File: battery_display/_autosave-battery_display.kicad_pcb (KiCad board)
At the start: 2 copper layers, 100 x 60 mm, 30 parts, among them J1 FH34SRJ-24S-0.5SH_99_, J2 Screw_Terminal_2x2.54, Q1 ZXM61N03F, Q2 ZXM61N03F, SW1 Button-THT - 2-1825910-7, U1 LDO40LPU33RY

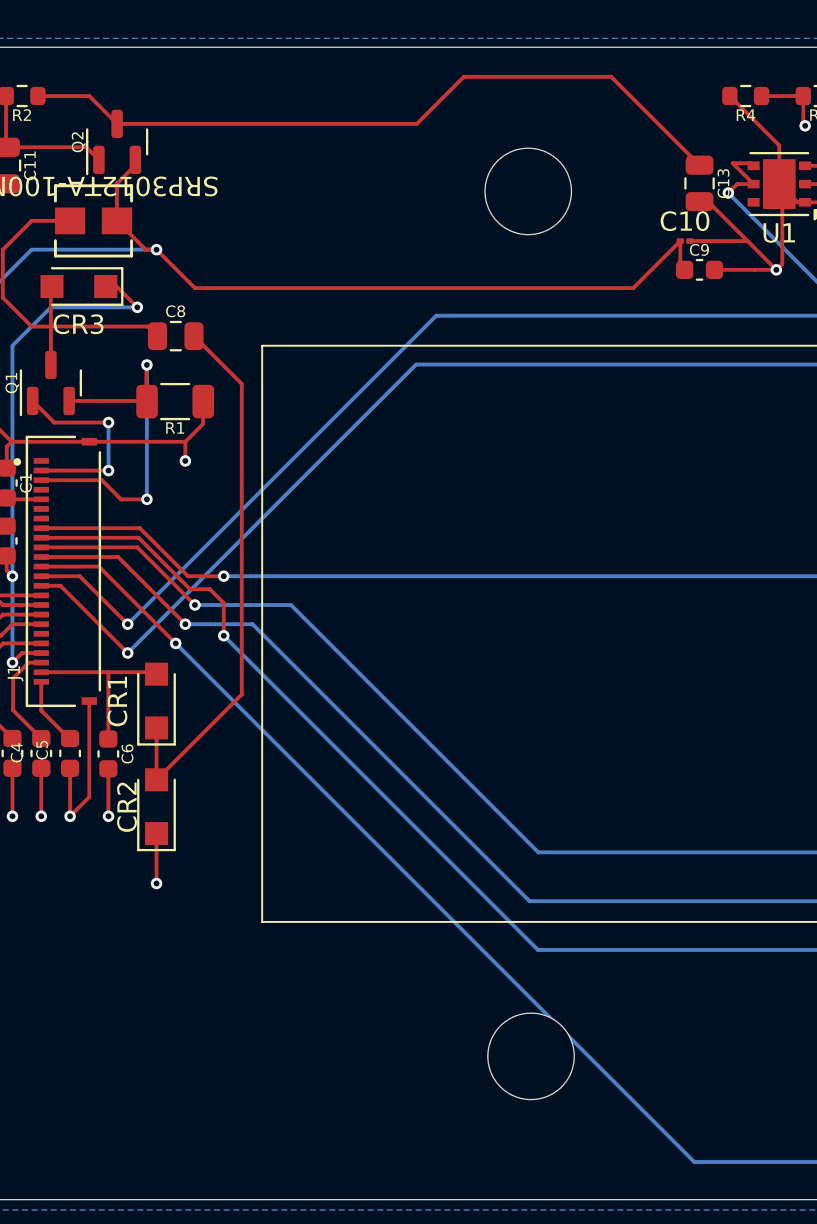
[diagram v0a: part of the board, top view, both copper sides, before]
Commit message: Adjusted drill hole placements (again)
Drill holes moved to be 30mm away from the left edge of the board
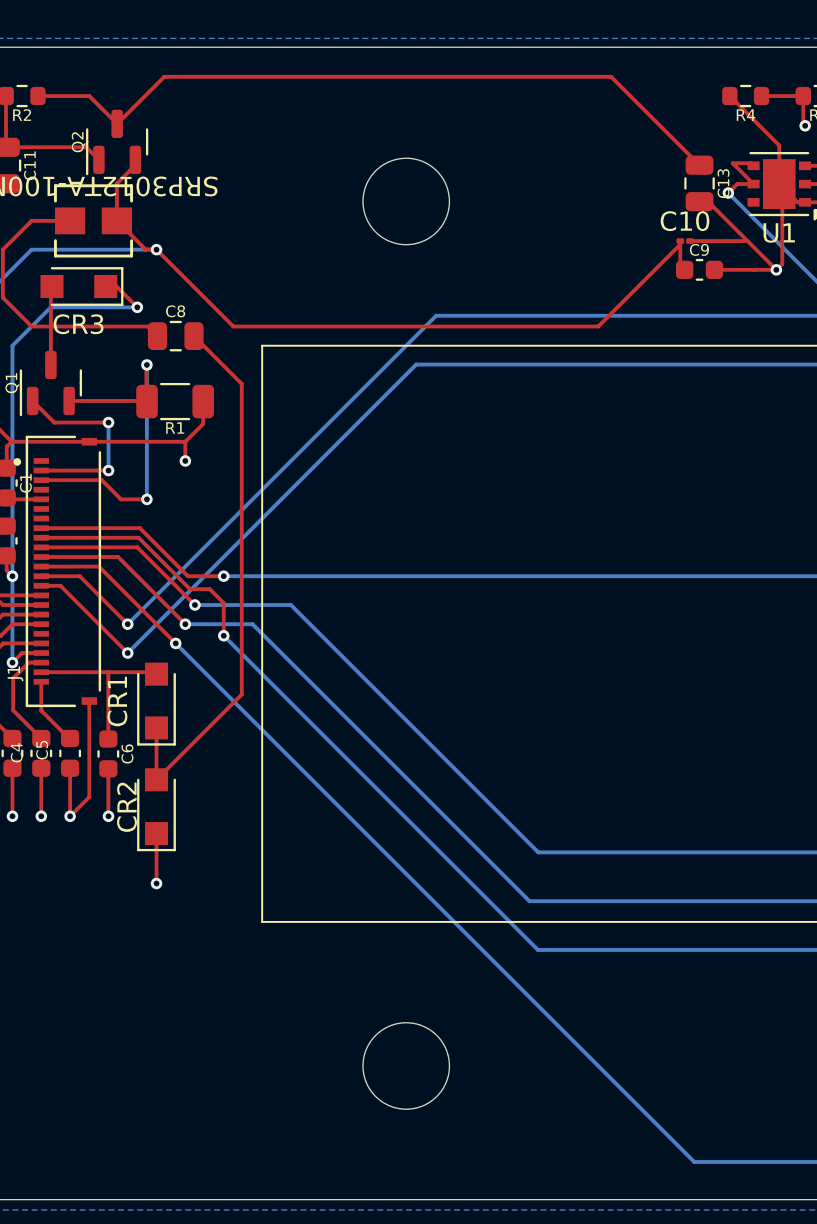
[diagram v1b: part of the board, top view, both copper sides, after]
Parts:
- moved H2 6.52 mm to (178.5, 83.0)
- moved H1 6.37 mm to (178.5, 38.0)
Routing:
- net /Display VDDD: track 67.5 -> 69.3 mm
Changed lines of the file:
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@@
 	(footprint "rsx_misc:MountingHole_4.5mm"
 		(layer "F.Cu")
-		(at 184.852431 37.467366)
+		(at 178.499999 37.989087)
 		(descr "Mounting Hole 4.5mm, no annular")
 		(tags "mounting hole 4.5mm no annular")
@@
 	(footprint "rsx_misc:MountingHole_4.5mm"
 		(layer "F.Cu")
-		(at 185 82.5)
+		(at 178.5 83)
 		(descr "Mounting Hole 4.5mm, no annular")
 		(tags "mounting hole 4.5mm no annular")
@@
 	)
 	(segment
-		(start 166.5 61)
-		(end 193.5 88)
+		(start 245.88 88)
+		(end 251.84 82.04)
 		(width 0.2)
 		(layer "B.Cu")
@@
 	)
 	(segment
-		(start 193.5 88)
-		(end 245.88 88)
+		(start 166.5 61)
+		(end 193.5 88)
 		(width 0.2)
 		(layer "B.Cu")
@@
 	)
 	(segment
-		(start 245.88 88)
-		(end 251.84 82.04)
+		(start 193.5 88)
+		(end 245.88 88)
 		(width 0.2)
 		(layer "B.Cu")
@@
 	)
 	(segment
-		(start 163.45 33.95)
-		(end 179.05 33.95)
+		(start 196.585 37.084)
+		(end 195.738 37.084)
+		(width 0.2)
+		(layer "F.Cu")
+		(net 66)
+	)
+	(segment
+		(start 193.772 36.1)
+		(end 189.172 31.5)
 		(width 0.2)
 		(layer "F.Cu")
@@
 	)
 	(segment
-		(start 196.585 37.084)
-		(end 195.738 37.084)
+		(start 165.9 31.5)
+		(end 163.45 33.95)
 		(width 0.2)
 		(layer "F.Cu")
@@
 	(segment
 		(start 189.172 31.5)
-		(end 193.772 36.1)
+		(end 165.9 31.5)
 		(width 0.2)
 		(layer "F.Cu")
@@
 	)
 	(segment
-		(start 179.05 33.95)
-		(end 181.5 31.5)
-		(width 0.2)
-		(layer "F.Cu")
-		(net 66)
-	)
-	(segment
-		(start 181.5 31.5)
-		(end 189.172 31.5)
-		(width 0.2)
-		(layer "F.Cu")
-		(net 66)
-	)
-	(segment
 		(start 162 32.5)
 		(end 163.45 33.95)
@@
 	)
 	(segment
-		(start 190.322 42.5)
-		(end 192.772 40.05)
+		(start 169.5 44.5)
+		(end 188.5 44.5)
 		(width 0.2)
 		(layer "F.Cu")
@@
 	)
 	(segment
-		(start 159.5 58.5)
-		(end 157 58.5)
+		(start 165.5 40.5)
+		(end 169.5 44.5)
 		(width 0.2)
 		(layer "F.Cu")
@@
 	)
 	(segment
-		(start 157.5 59)
-		(end 159.5 59)
+		(start 159.5 58.5)
+		(end 157 58.5)
 		(width 0.2)
 		(layer "F.Cu")
@@
 	)
 	(segment
-		(start 165.5 40.5)
-		(end 167.5 42.5)
+		(start 157.5 59)
+		(end 159.5 59)
 		(width 0.2)
 		(layer "F.Cu")
@@
 	)
 	(segment
-		(start 164.4 35.825)
-		(end 164.4 36.1)
+		(start 192.772 40.228)
+		(end 192.772 40.05)
 		(width 0.2)
 		(layer "F.Cu")
@@
 	)
 	(segment
-		(start 167.5 42.5)
-		(end 190.322 42.5)
+		(start 164.4 35.825)
+		(end 164.4 36.1)
 		(width 0.2)
 		(layer "F.Cu")
@@
 		(width 0.2)
 		(layer "F.Cu")
+		(net 75)
+	)
+	(segment
+		(start 188.5 44.5)
+		(end 192.772 40.228)
+		(width 0.2)
+		(layer "F.Cu")

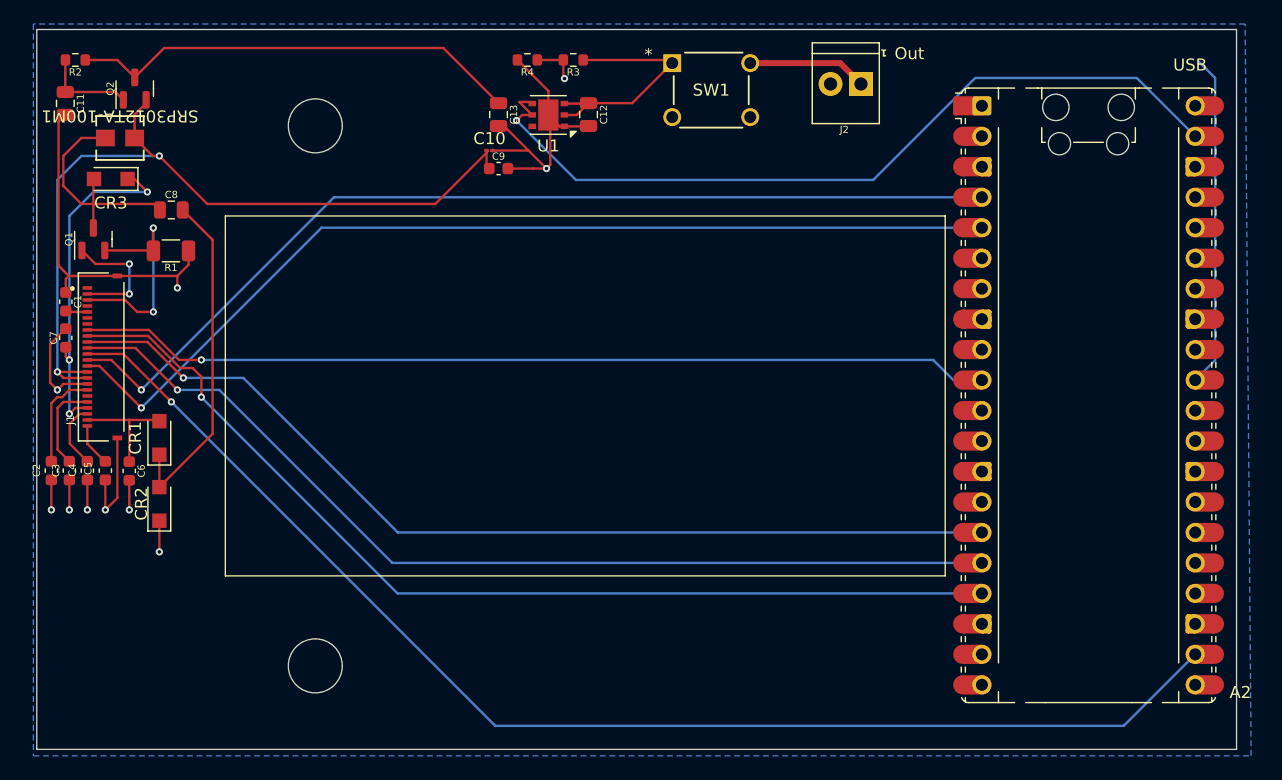
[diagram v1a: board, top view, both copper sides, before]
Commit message: changed wire connections
changed back side wires to front side wires to avoid back side copper islanding
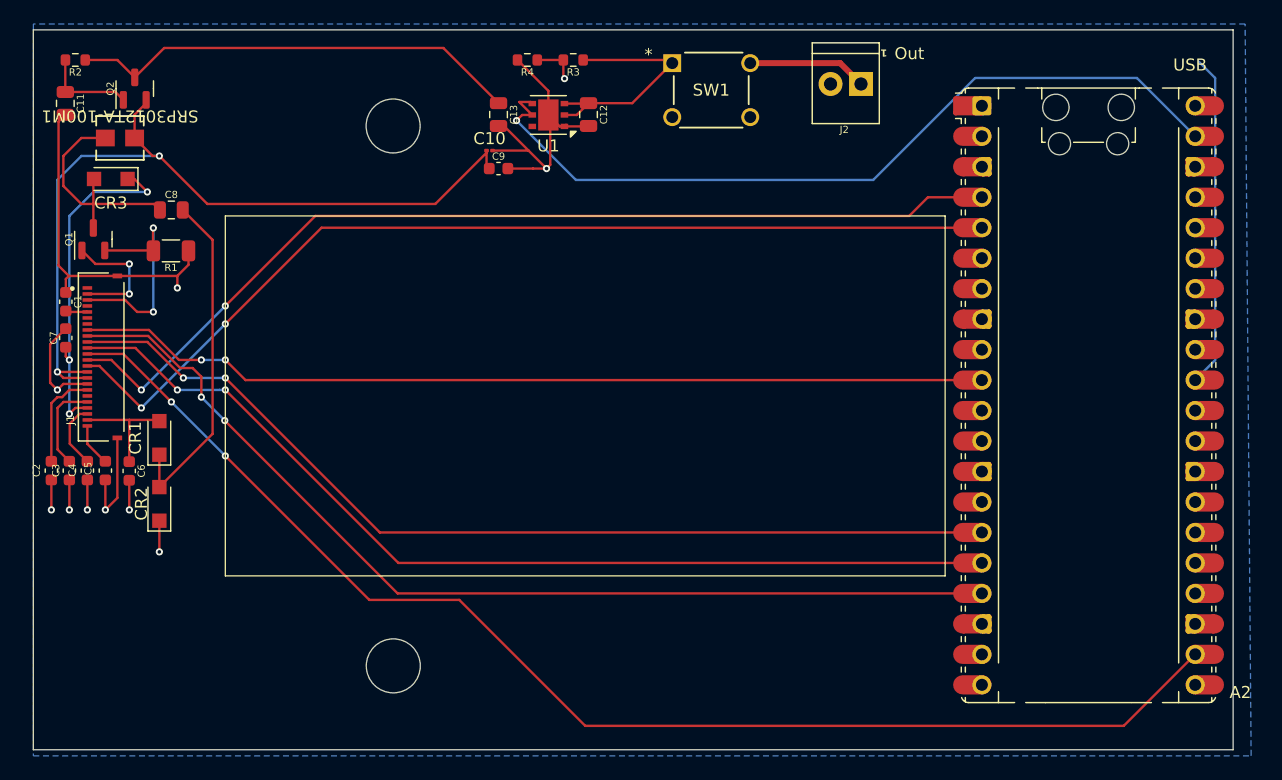
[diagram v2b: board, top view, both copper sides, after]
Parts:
- moved H2 6.50 mm to (185.0, 83.0)
- moved H1 6.48 mm to (185.0, 38.0)
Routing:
- net /BS: track 76.3 -> 78.7 mm, vias 1 -> 2
- net /panelDC: vias 1 -> 2
- net /panelBusy: vias 1 -> 2
- net /panelReset: vias 1 -> 2
- net /panelCS: vias 1 -> 2
- net /SDA: vias 1 -> 2
- net /SCLK: vias 1 -> 2
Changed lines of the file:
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@@
 	(footprint "rsx_misc:MountingHole_4.5mm"
 		(layer "F.Cu")
-		(at 178.499999 37.989087)
+		(at 184.984808 37.999897)
 		(descr "Mounting Hole 4.5mm, no annular")
 		(tags "mounting hole 4.5mm no annular")
@@
 	(footprint "rsx_misc:MountingHole_4.5mm"
 		(layer "F.Cu")
-		(at 178.5 83)
+		(at 185 83)
 		(descr "Mounting Hole 4.5mm, no annular")
 		(tags "mounting hole 4.5mm no annular")
@@
 	)
 	(gr_rect
-		(start 155.285 29.96)
-		(end 255.285 89.96)
+		(start 154.998055 29.99047)
+		(end 254.998055 89.99047)
 		(stroke
 			(width 0.05)
@@
 	)
 	(segment
+		(start 228 45.5)
+		(end 229.56 43.94)
+		(width 0.2)
+		(layer "F.Cu")
+		(net 27)
+	)
+	(segment
 		(start 161.5 57.5)
 		(end 164 60)
@@
 	)
 	(segment
+		(start 171 53)
+		(end 178.5 45.5)
+		(width 0.2)
+		(layer "F.Cu")
+		(net 27)
+	)
+	(segment
+		(start 229.56 43.94)
+		(end 234.06 43.94)
+		(width 0.2)
+		(layer "F.Cu")
+		(net 27)
+	)
+	(segment
+		(start 178.5 45.5)
+		(end 228 45.5)
+		(width 0.2)
+		(layer "F.Cu")
+		(net 27)
+	)
+	(segment
 		(start 159.5 57.5)
 		(end 161.5 57.5)
@@
 	)
 	(via
+		(at 171 53)
+		(size 0.6)
+		(drill 0.3)
+		(layers "F.Cu" "B.Cu")
+		(net 27)
+	)
+	(via
 		(at 164 60)
 		(size 0.6)
@@
 	)
 	(segment
-		(start 180.06 43.94)
-		(end 234.06 43.94)
+		(start 164 60)
+		(end 171 53)
 		(width 0.2)
 		(layer "B.Cu")
@@
 	)
 	(segment
-		(start 164 60)
-		(end 180.06 43.94)
+		(start 183 77.5)
+		(end 190.5 77.5)
 		(width 0.2)
-		(layer "B.Cu")
-		(net 27)
+		(layer "F.Cu")
+		(net 29)
 	)
 	(segment
@@
 	)
 	(segment
+		(start 245.88 88)
+		(end 251.84 82.04)
+		(width 0.2)
+		(layer "F.Cu")
+		(net 29)
+	)
+	(segment
 		(start 162.5 57)
 		(end 159.5 57)
@@
 		(net 29)
 	)
+	(segment
+		(start 190.5 77.5)
+		(end 201 88)
+		(width 0.2)
+		(layer "F.Cu")
+		(net 29)
+	)
+	(segment
+		(start 201 88)
+		(end 245.88 88)
+		(width 0.2)
+		(layer "F.Cu")
+		(net 29)
+	)
+	(segment
+		(start 171 65.5)
+		(end 183 77.5)
+		(width 0.2)
+		(layer "F.Cu")
+		(net 29)
+	)
 	(via
 		(at 166.5 61)
@@
 		(net 29)
 	)
-	(segment
-		(start 245.88 88)
-		(end 251.84 82.04)
-		(width 0.2)
-		(layer "B.Cu")
+	(via
+		(at 171 65.5)
+		(size 0.6)
+		(drill 0.3)
+		(layers "F.Cu" "B.Cu")
 		(net 29)
 	)
 	(segment
 		(start 166.5 61)
-		(end 193.5 88)
+		(end 171 65.5)
 		(width 0.2)
 		(layer "B.Cu")
@@
 	)
 	(segment
-		(start 193.5 88)
-		(end 245.88 88)
+		(start 163.5 56.5)
+		(end 159.5 56.5)
 		(width 0.2)
-		(layer "B.Cu")
-		(net 29)
+		(layer "F.Cu")
+		(net 32)
 	)
 	(segment
-		(start 163.5 56.5)
-		(end 159.5 56.5)
+		(start 185.42 74.42)
+		(end 234.06 74.42)
 		(width 0.2)
 		(layer "F.Cu")
@@
 		(net 32)
 	)
+	(segment
+		(start 171 60)
+		(end 185.42 74.42)
+		(width 0.2)
+		(layer "F.Cu")
+		(net 32)
+	)
+	(via
+		(at 171 60)
+		(size 0.6)
+		(drill 0.3)
+		(layers "F.Cu" "B.Cu")
+		(net 32)
+	)
 	(via
 		(at 167 60)
@@
 	)
 	(segment
-		(start 234.06 74.42)
-		(end 184.92 74.42)
+		(start 170.5 60)
+		(end 171 60)
 		(width 0.2)
 		(layer "B.Cu")
@@
 	)
 	(segment
-		(start 184.92 74.42)
-		(end 170.5 60)
+		(start 179.02 46.48)
+		(end 234.06 46.48)
+		(width 0.2)
+		(layer "F.Cu")
+		(net 43)
+	)
+	(segment
+		(start 171 54.5)
+		(end 179.02 46.48)
 		(width 0.2)
-		(layer "B.Cu")
-		(net 32)
+		(layer "F.Cu")
+		(net 43)
 	)
 	(segment
@@
 	)
 	(via
-		(at 164 61.5)
+		(at 171 54.5)
 		(size 0.6)
 		(drill 0.3)
@@
 		(net 43)
 	)
-	(segment
-		(start 179.02 46.48)
-		(end 234.06 46.48)
-		(width 0.2)
-		(layer "B.Cu")
+	(via
+		(at 164 61.5)
+		(size 0.6)
+		(drill 0.3)
+		(layers "F.Cu" "B.Cu")
 		(net 43)
 	)
 	(segment
 		(start 164 61.5)
-		(end 179.02 46.48)
+		(end 171 54.5)
 		(width 0.2)
 		(layer "B.Cu")
@@
 		(net 49)
 	)
+	(segment
+		(start 183.88 71.88)
+		(end 234.06 71.88)
+		(width 0.2)
+		(layer "F.Cu")
+		(net 49)
+	)
+	(segment
+		(start 171 59)
+		(end 183.88 71.88)
+		(width 0.2)
+		(layer "F.Cu")
+		(net 49)
+	)
 	(via
-		(at 167.5 59)
+		(at 171 59)
 		(size 0.6)
 		(drill 0.3)
@@
 		(net 49)
 	)
-	(segment
-		(start 234.06 71.88)
-		(end 185.38 71.88)
-		(width 0.2)
-		(layer "B.Cu")
+	(via
+		(at 167.5 59)
+		(size 0.6)
+		(drill 0.3)
+		(layers "F.Cu" "B.Cu")
 		(net 49)
 	)
 	(segment
-		(start 172.5 59)
+		(start 171 59)
 		(end 167.5 59)
 		(width 0.2)
@@
 	)
 	(segment
-		(start 185.38 71.88)
-		(end 172.5 59)
+		(start 171 57.5)
+		(end 172.68 59.18)
 		(width 0.2)
-		(layer "B.Cu")
-		(net 49)
+		(layer "F.Cu")
+		(net 56)
 	)
 	(segment
@@
 		(net 56)
 	)
+	(segment
+		(start 172.68 59.18)
+		(end 234.06 59.18)
+		(width 0.2)
+		(layer "F.Cu")
+		(net 56)
+	)
+	(via
+		(at 171 57.5)
+		(size 0.6)
+		(drill 0.3)
+		(layers "F.Cu" "B.Cu")
+		(net 56)
+	)
 	(via
 		(at 169 57.5)
@@
 	)
 	(segment
-		(start 231.68 59.18)
-		(end 230 57.5)
-		(width 0.2)
-		(layer "B.Cu")
-		(net 56)
-	)
-	(segment
-		(start 230 57.5)
-		(end 169 57.5)
+		(start 169 57.5)
+		(end 171 57.5)
 		(width 0.2)
 		(layer "B.Cu")
@@
 	)
 	(segment
+		(start 185.36 76.96)
+		(end 234.06 76.96)
+		(width 0.2)
+		(layer "F.Cu")
+		(net 58)
+	)
+	(segment
 		(start 167.241365 58.174265)
 		(end 168.274265 58.174265)
@@
 		(net 58)
 	)
+	(segment
+		(start 170.95 62.55)
+		(end 185.36 76.96)
+		(width 0.2)
+		(layer "F.Cu")
+		(net 58)
+	)
 	(via
-		(at 169 60.6)
+		(at 170.95 62.55)
 		(size 0.6)
 		(drill 0.3)
@@
 		(net 58)
 	)
-	(segment
-		(start 169 60.6)
-		(end 185.36 76.96)
-		(width 0.2)
-		(layer "B.Cu")
+	(via
+		(at 169 60.6)
+		(size 0.6)
+		(drill 0.3)
+		(layers "F.Cu" "B.Cu")
 		(net 58)
 	)
 	(segment
-		(start 185.36 76.96)
-		(end 234.06 76.96)
+		(start 169 60.6)
+		(end 170.95 62.55)
 		(width 0.2)
 		(layer "B.Cu")
